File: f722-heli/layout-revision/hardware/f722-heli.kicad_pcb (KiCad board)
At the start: 6 copper layers, 41.7 x 25.4 mm, 156 parts, among them J1 USB4145-03-0170-C, J10 PORT B / JST GH, J11 PORT C / JST GH, J12 DSM / JST ZH, J2 S1 / GND-VX-S, J3 S2 / GND-VX-S, J4 S3 / GND-VX-S, J5 TAIL / GND-VX-S, J6 ESC / GND-VX-S, J7 RPM / GND-VX-S, J8 SBUS / GND-VX-S, J9 PORT A / JST GH, Q1 BSS138LT1G, Q2 BSS138LT1G, SW1 BOOT / KMT031NGJLHS, U1 STM32F722RET6, U10 TPS2553DRVR / USB input limit, U11 TPS2553DRVR / DSM output limit, U12 USBLC6-4SC6 / header clamp, U13 USBLC6-4SC6 / header clamp, U14 TPD4E05U06DQAR / UART ESD, U15 TPD4E05U06DQAR / UART ESD, U16 PESD15VS2UT,215 / 15V ESD, U2 ICM-42688-P, U3 W25N01GVZEIG / 128MiB, U4 DPS368XTSA1 / 0x76, U5 TPS259472ARPWR, U6 TPS63070RNMR / nominal 5.088V, U7 TPS2117DRLR / ABC priority mux, U8 TPS2121RUXR / BEC-priority co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, U9 TPS62162DSGR / 3.3V 1A, Y1 8MHz / CL10pF / TAXM8M4RDBCCT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

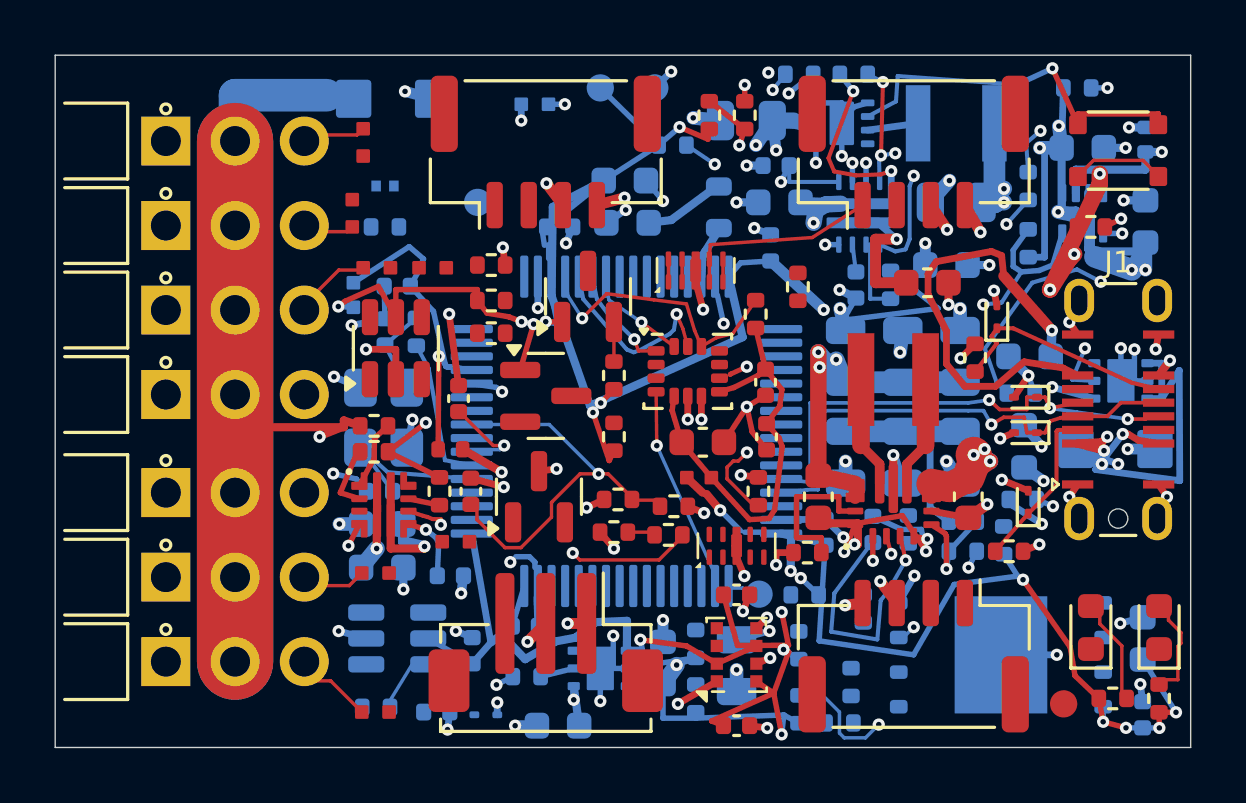
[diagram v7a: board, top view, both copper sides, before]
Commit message: WIP: checkpoint F722 routing at 55 unfinished connections
Current numerical power/VCAP validation not run after changed fills. Historical results do not qualify this board. Not for fabrication or flight.
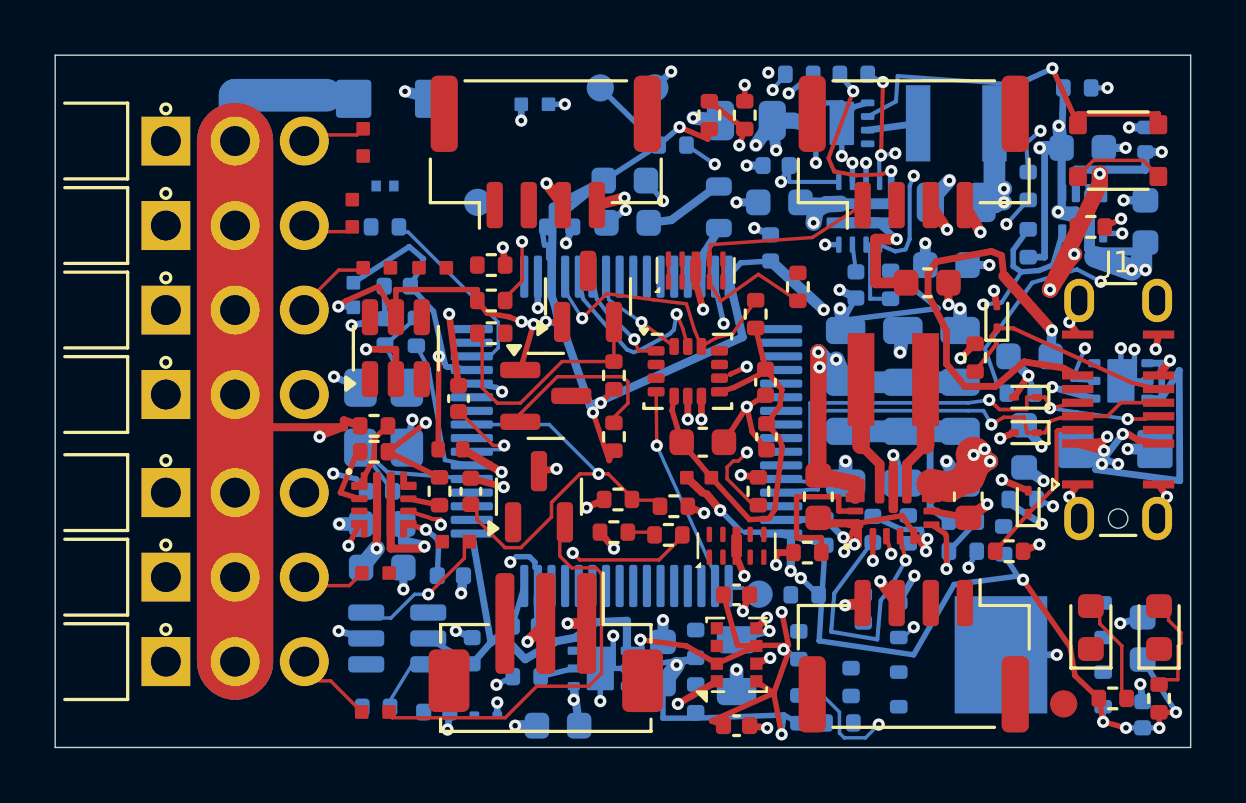
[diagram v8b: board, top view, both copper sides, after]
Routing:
- net SBUS_HV: track 0.00 -> 14.6 mm
- net NRST: track 2.49 -> 12.8 mm, vias 1 -> 2
- net SBUS_LV: track 0.60 -> 7.82 mm
- net PORT_A_RX_MCU: track 0.00 -> 6.41 mm
- net RPM_LV: track 0.00 -> 6.41 mm
- net ESC_MCU: track 0.00 -> 4.39 mm, vias 0 -> 1
- net PORT_B_RX_EXT: track 7.31 -> 11.6 mm
